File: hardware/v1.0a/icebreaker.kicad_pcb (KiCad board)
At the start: 4 copper layers, 73 x 37 mm, 128 parts, among them J1 Jumper, J10 Jumper, J11 Jumper, J12 Jumper, J13 Jumper, J14 Jumper, J15 Jumper, J16 Jumper, J17 Jumper, J18 Jumper, J19 Jumper, J2 Jumper, J20 Flash, J21 PMOD, J22 PMOD, J23 PMOD, J24 PMOD, J25 RGB Led, J26 5V AUX, J27 5V AUX, J28 CRESET, J3 Jumper, J4 Jumper, J5 Jumper, J6 Jumper, J7 Jumper, J8 Jumper, J9 Jumper, P1 pkl_USB_OTG, P2 UP, P3 UP, P4 UP, P5 UP, SW1 TACT, SW2 TACT, SW3 TACT, SW4 TACT, U1 93C46B-SOT-23-6, U2 3.3V, U3 1V2, U4 FT2232H, U5 W25Q, U6 ICE5LP4K-SG48, U7 12MHz

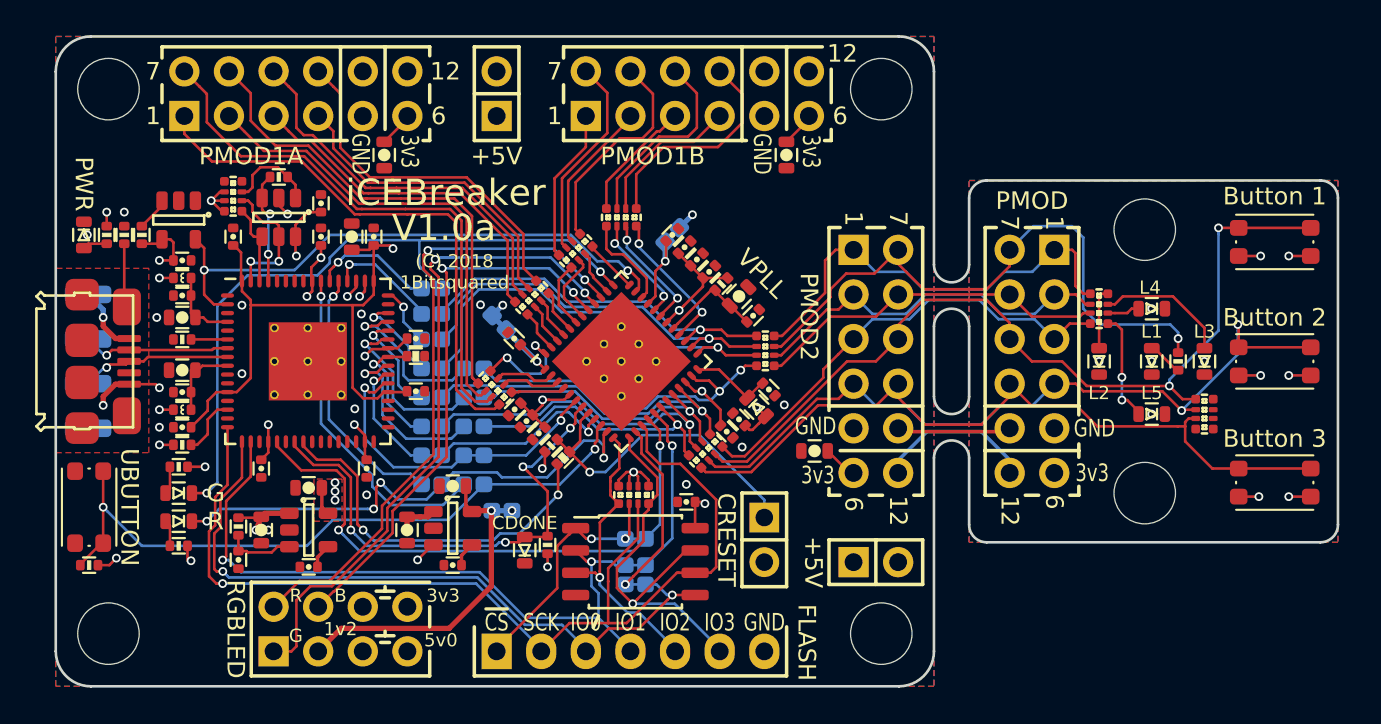
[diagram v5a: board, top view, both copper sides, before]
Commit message: Updated all design files to KiCad V8.0.6.
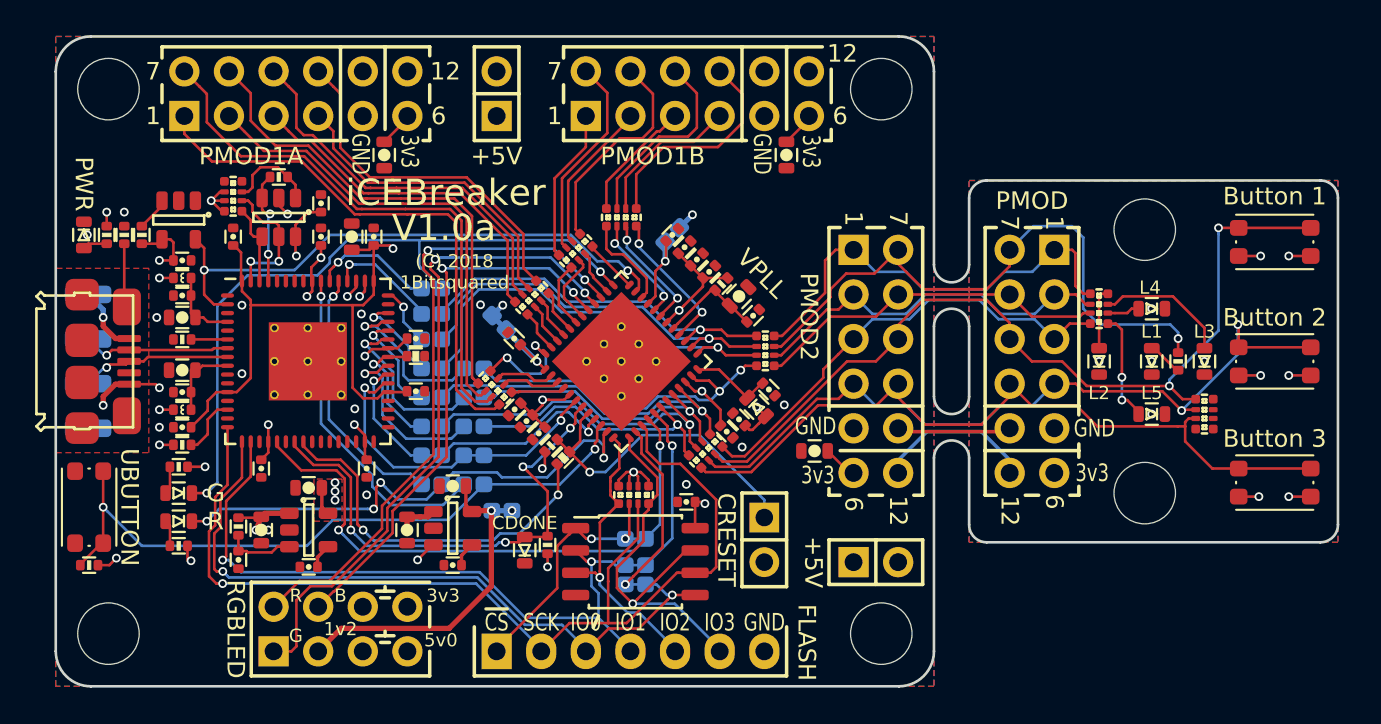
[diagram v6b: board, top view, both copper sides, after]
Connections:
- net /FLASH_~HLD~|~RST~|IO3 renamed /FLASH_~{HLD}|~{RST}|IO3
- net /FLASH_~WP~|IO2 renamed /FLASH_~{WP}|IO2
- net /xFIFO_~RD renamed /xFIFO_~{RD}
- net /xFIFO_~RXF renamed /xFIFO_~{RXF}
- net /xFIFO_~TXE renamed /xFIFO_~{TXE}
- net /xFIFO_~WR renamed /xFIFO_~{WR}
- net /~BUTTON renamed /~{BUTTON}
- net /~LEDG renamed /~{LEDG}
- net /~LEDR renamed /~{LEDR}
- net /~LED_BLU renamed /~{LED_BLU}
- net /~LED_GRN renamed /~{LED_GRN}
- net /~LED_RED renamed /~{LED_RED}
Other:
- net class Default removed
- board text added: "~{CS}"
- board text removed: "~CS"
